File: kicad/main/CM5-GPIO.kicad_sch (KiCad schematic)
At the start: 19 parts, among them Q13 IRLML6344TRPBF, Q18 IRLML6344TRPBF, U3 74LVC1G07GW_125, U6 RT9742GGJ5

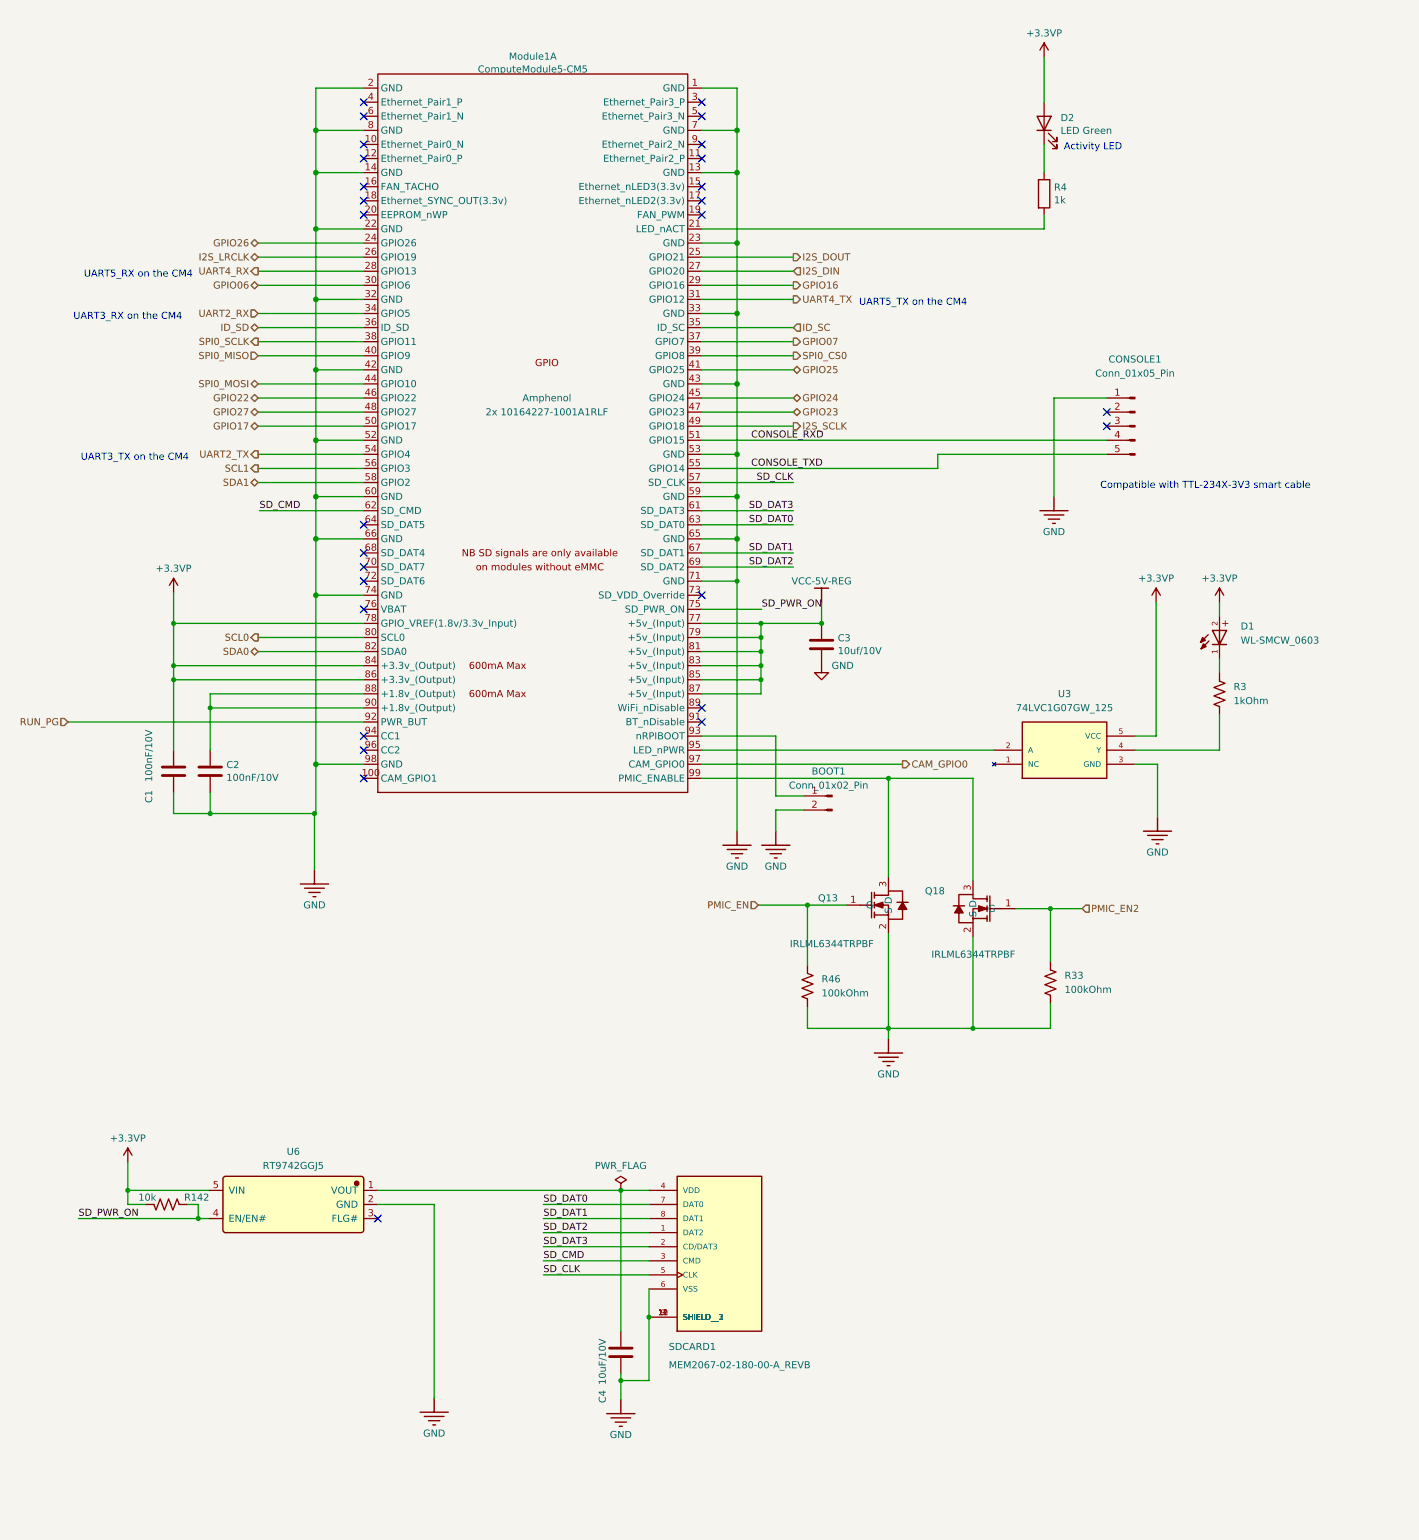
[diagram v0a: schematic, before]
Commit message: Fix edge cut; no-CM STEP
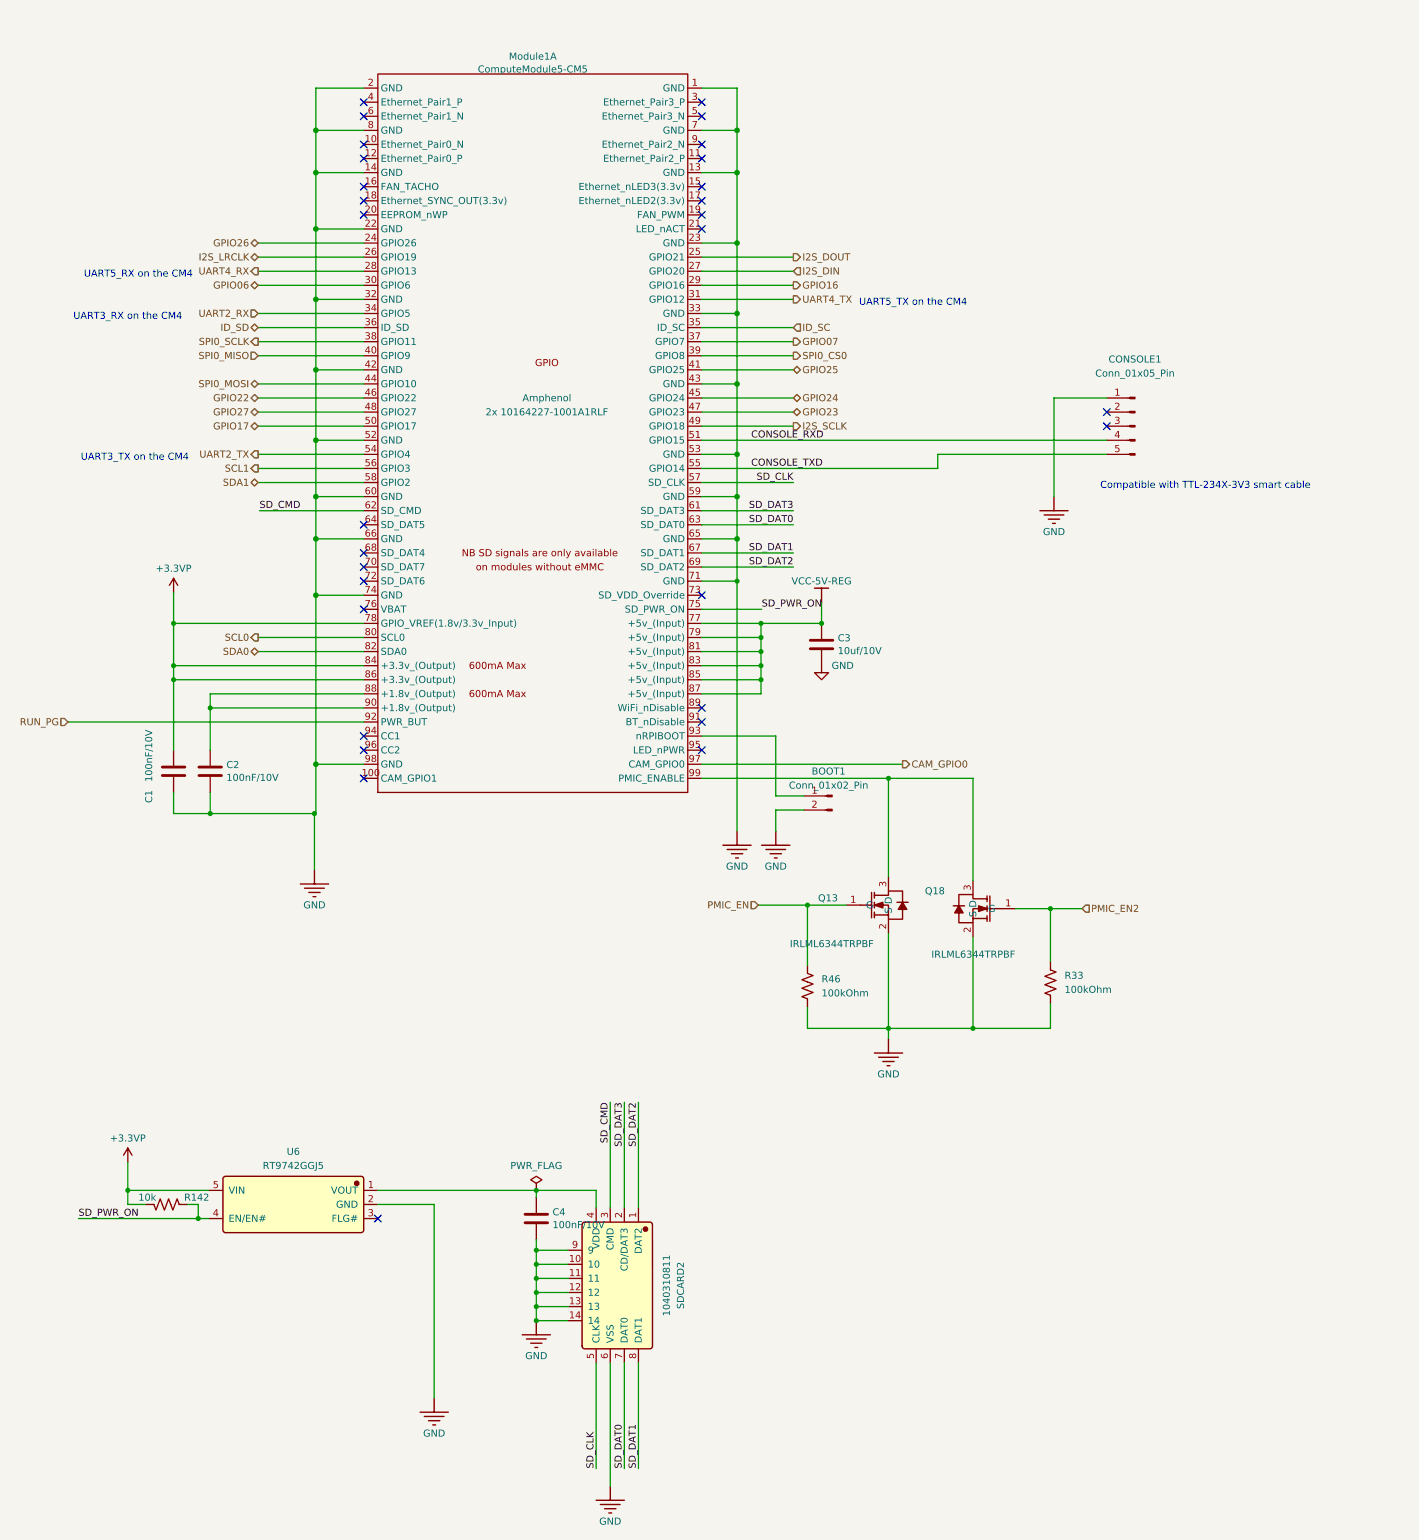
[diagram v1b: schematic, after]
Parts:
- removed D1: WL-SMCW_0603, WL-SMCW_0603:WL-SMCW_0603, symbol WL-SMCW_0603:WL-SMCW_0603
- removed D2: LED Green, LED_SMD:LED_0603_1608Metric, symbol Device:LED
- removed R3: 1kOhm, Resistor_SMD:R_0603_1608Metric_Pad0.98x0.95mm_HandSolder, symbol Device:R_US
- removed R4: 1k, Resistor_SMD:R_0603_1608Metric_Pad0.98x0.95mm_HandSolder, symbol Device:R
- removed SDCARD1: MEM2067-02-180-00-A_REVB, MEM2067-02-180-00-A_REVB:GCT_MEM2067-02-180-00-A_REVB, symbol MEM2067-02-180-00-A_REVB:MEM2067-02-180-00-A_REVB
- removed U3: 74LVC1G07GW_125, 74LVC1G07GW_125:IC_74LVC1G07GW_125, symbol 74LVC1G07GW_125:74LVC1G07GW_125
- added SDCARD2: 1040310811, JLCImport:1040310811, symbol JLCImport:1040310811
- C1, C2, C3: footprint Capacitor_SMD:C_0603_1608Metric_Pad1.08x0.95mm_HandSolder -> Capacitor_SMD:C_0603_1608Metric
- C4: value 10uF/10V -> 100nF/10V; footprint Capacitor_SMD:C_0603_1608Metric_Pad1.08x0.95mm_HandSolder -> Capacitor_SMD:C_0603_1608Metric; Field4 (none) -> Farnell; Field5 (none) -> 2611911; Field6 (none) -> RM EMK105 B7104KV-F; Field7 (none) -> TAIYO YUDEN EUROPE GMBH; Field8 (none) -> 110091611; Part Description (none) -> 0.1uF 10% 16V Ceramic Capacitor X7R 0402 (1005 Metric)
- CONSOLE1: footprint (none) -> Connector_PinHeader_2.54mm:PinHeader_1x05_P2.54mm_Vertical
- R33, R46: footprint Resistor_SMD:R_0603_1608Metric_Pad0.98x0.95mm_HandSolder -> Resistor_SMD:R_0603_1608Metric
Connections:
- net GND: now also SDCARD2.10, SDCARD2.11, SDCARD2.12, SDCARD2.13, SDCARD2.14, SDCARD2.6 (VSS), SDCARD2.9
- net SD_CLK: now also SDCARD2.5 (CLK)
- net SD_CMD: now also SDCARD2.3 (CMD)
- net SD_DAT0: now also SDCARD2.7 (DAT0)
- net SD_DAT1: now also SDCARD2.8 (DAT1)
- net SD_DAT2: now also SDCARD2.1 (DAT2)
- net SD_DAT3: now also SDCARD2.2 (CD/DAT3)
- net at C4.1, U6.1 (VOUT): now also SDCARD2.4 (VDD)
- no-connect marks 28 -> 30
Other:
- note removed: "Activity LED"

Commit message: Schematic fixes, 1st round of review
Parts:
- removed Q13, Q18: IRLML6344TRPBF, JLCImport:IRLML6344TRPBF, symbol JLCImport:IRLML6344TRPBF
- removed R33, R46: 100kOhm, Resistor_SMD:R_0603_1608Metric, symbol Device:R_US
- added CM_ACT1, CM_PWR1: YLED0603B, JLCImport:YLED0603B, symbol JLCImport:YLED0603B
- added H1: PM254-2-06-S-8_5, JLCImport:PM254-2-06-S-8_5, symbol JLCImport:PM254-2-06-S-8_5
- added Q10: 2302V, JLCImport:2302V, symbol JLCImport:2302V
- added R82, R85: 1k, Resistor_SMD:R_0603_1608Metric, symbol Device:R_US
- BOOT1: LCSC (none) -> C32713268
- C1, C2, C4: value 100nF/10V -> 100nF/50V; LCSC (none) -> C1591
- C3: value 10uf/10V -> 10uF/25V; LCSC (none) -> C96446
- CONSOLE1: LCSC (none) -> C42431835
- Module1: LCSC (none) -> 2X C6932320
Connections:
- net +3.3VP: now also R82.1, R85.1
- net GND: now also H1.12, Q10.2 (S)
- net GPIO22: now also H1.5
- net GPIO23: now also H1.8
- net GPIO24: now also H1.7
- net PMIC_EN: now also Module1.99 (PMIC_ENABLE)
- net CAM_GPIO1: now reaches Module1.100 (CAM_GPIO1)
- net at Module1.21 (LED_nACT): now also CM_ACT1.2 (K)
- net at Module1.95 (LED_nPWR): now also Q10.1 (G)
- net GPIO07 renamed GPIO7
- net GPIO7: now also H1.2
- net SPI0_CS0 renamed GPIO8
- net GPIO8: now also H1.1
- net SPI0_MISO renamed GPIO9
- net GPIO9: now also H1.4
- net SPI0_MOSI renamed GPIO10
- net GPIO10: now also H1.3
- net SPI0_SCLK renamed GPIO11
- net GPIO11: now also H1.6
- net UART4_RX renamed GPIO13
- net GPIO13: now also H1.10
- net UART4_TX renamed GPIO12
- net GPIO12: now also H1.9
- new net: CM_PWR1.1 (A), R82.2
- new net: CM_PWR1.2 (K), Q10.3 (D)
- new net: CM_ACT1.1 (A), R85.2
- new net VCC3V3_M2: H1.11
- no-connect marks 30 -> 27
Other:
- note removed: "UART5_RX on the CM4"
- note removed: "UART5_TX on the CM4"
